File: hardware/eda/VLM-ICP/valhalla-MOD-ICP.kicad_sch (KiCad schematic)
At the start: 6 parts, among them J1 BUS, J2 AVR-ISP-6

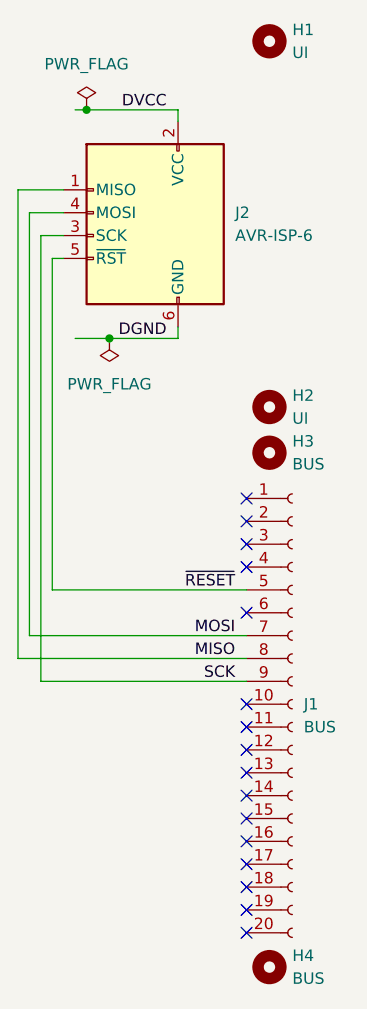
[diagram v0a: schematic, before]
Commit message: BUGFIX: missing power net connections on MOD-ICSP schematic
  - as it happens, the layout was correct "by mistake" since it had
    been instantiated from the template and never updated, and as
    such the power connections were still present on the BUS
    connector.
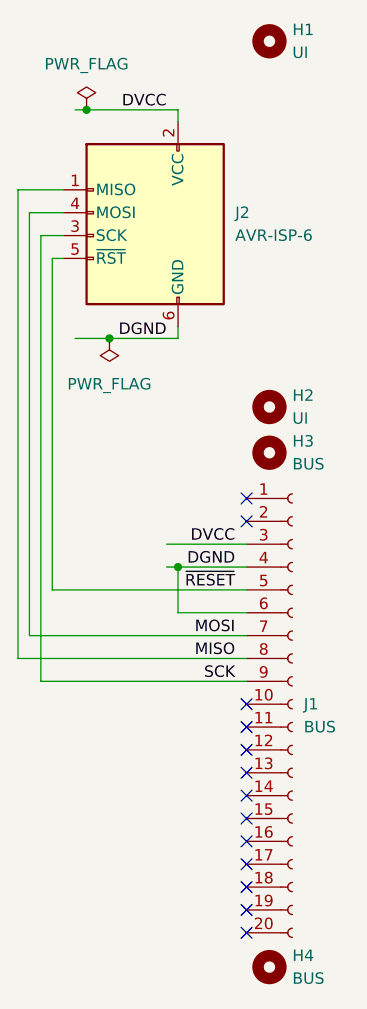
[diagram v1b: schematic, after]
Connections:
- net DGND: now also J1.4 (Pin_4), J1.6 (Pin_6)
- net DVCC: now also J1.3 (Pin_3)
- no-connect marks 16 -> 13
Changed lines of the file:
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@@
 (kicad_sch
-	(version 20231120)
+	(version 20250114)
 	(generator "eeschema")
-	(generator_version "8.0")
+	(generator_version "9.0")
 	(paper "A4")
 	(title_block
 		(title "Atmel ICSP interface for CPU(ATMega)")
-		(date "2025-02-02")
-		(rev "1")
+		(date "2025-03-25")
+		(rev "2")
+	)
+	(junction
+		(at 262.89 76.2)
+		(diameter 0)
+		(color 0 0 0 0)
 	)
 	(junction
@@
 	)
 	(no_connect
-		(at 270.51 81.28)
-	)
-	(no_connect
 		(at 270.51 68.58)
 	)
@@
 	)
 	(no_connect
-		(at 270.51 76.2)
-	)
-	(no_connect
-		(at 270.51 73.66)
-	)
-	(no_connect
 		(at 270.51 116.84)
 	)
@@
 	(wire
 		(pts
+			(xy 261.62 76.2) (xy 262.89 76.2)
+		)
+		(stroke
+			(width 0)
+			(type default)
+		)
+	)
+	(wire
+		(pts
+			(xy 261.62 73.66) (xy 270.51 73.66)
+		)
+		(stroke
+			(width 0)
+			(type default)
+		)
+	)
+	(wire
+		(pts
 			(xy 245.11 34.29) (xy 245.11 86.36)
 		)
@@
 	(wire
 		(pts
+			(xy 270.51 81.28) (xy 262.89 81.28)
+		)
+		(stroke
+			(width 0)
+			(type default)
+		)
+	)
+	(wire
+		(pts
 			(xy 248.92 78.74) (xy 270.51 78.74)
 		)
@@
 	(wire
 		(pts
+			(xy 262.89 76.2) (xy 270.51 76.2)
+		)
+		(stroke
+			(width 0)
+			(type default)
+		)
+	)
+	(wire
+		(pts
 			(xy 250.19 34.29) (xy 245.11 34.29)
+		)
+		(stroke
+			(width 0)
+			(type default)
+		)
+	)
+	(wire
+		(pts
+			(xy 262.89 81.28) (xy 262.89 76.2)
 		)
 		(stroke
@@
 	(label "~{RESET}"
 		(at 269.24 78.74 180)
+		(effects
+			(font
+				(size 1.27 1.27)
+			)
+			(justify right bottom)
+		)
+	)
+	(label "DGND"
+		(at 269.24 76.2 180)
+		(effects
+			(font
+				(size 1.27 1.27)
+			)
+			(justify right bottom)
+		)
+	)
+	(label "DVCC"
+		(at 269.24 73.66 180)
 		(effects
 			(font
@@
 		)
 	)
+	(embedded_fonts no)
 )

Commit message: UPDATE: cosmetic fixes to schematic defaults
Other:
- title: Atmel ICSP interface for CPU(ATMega) -> Valhalla MOD-ICP(AVR-ICSP)
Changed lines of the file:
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@@
 	(paper "A4")
 	(title_block
-		(title "Atmel ICSP interface for CPU(ATMega)")
+		(title "Valhalla MOD-ICP(AVR-ICSP)")
 		(date "2025-03-25")
 		(rev "2")
